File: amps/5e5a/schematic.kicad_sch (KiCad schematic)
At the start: 63 parts, among them T1 PT, T2 ~4.3k:8

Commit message: Fix: the 6G5's rectifier was connected to nothing; 17 sheets shorted the mains by naming both leads alike
6G5 power supply. The sheet drew four diodes as a "silicon bridge" whose
HT_A/HT_B labels stopped 6 mm short of their wires. D1/D2's anodes sat on
the tremolo's cathode node (a tremolo wire's end touched the old diode
stub), D3/D4 ran from ground to the reservoir, and TR1's centre tap floated
under an open-pin waiver whose stated reason was the bridge itself.
A-FJ (Schematic Heaven 2153x1437, read enlarged): each HT end of TR1 runs
through a leg of three silicon diodes, every + (cathode) toward the +460 V
reservoir; the centre tap is grounded; TR1's second secondary terminal is a
bias tap feeding the 6G4's network part for part: rectifier, 8-150, 10K,
then 8-150 and a 56K bleeder at the -55 V line. Redrawn as the drawing
shows: D1-D6, TR1 with its tap pin, the centre tap to ground, the bias
network (CBIAS 25 uF -> 8 uF; RBIAS2, CBIAS2, RBIAS1 added), the waiver
deleted, and the notes, meta, netlist header and parts list no longer say
bridge. Not yet carried: the drawing's second 20-600 at the reservoir and
the standby switch (this sheet omits chassis switches by its own note);
and the tremolo ladder still runs through the transformer's corner of the
sheet, a layout clash rather than a connection, queued for its own redraw.

Mains. Two global labels with one name are one net. 16 of 24 power
transformers on the sheets carried a label named MAINS on both primary
leads, so the winding's two pins were one net: 5E4-A, 5E5-A, 5F4, 5G9,
6161, 6G2, 6G3, 6G4, AA1164, AA764, AA764-Vibro, AA964, AB763, AB763
Super, AB763 Twin, GA-40. The 6G5's loop ran from one MAINS label through
switch, fuse and winding back to the same name. No gate models the primary,
so a copy-pasted idiom did this. The second lead is now MAINS N, the AC15's
idiom; the AA1164's and AA964's second AC row, drawn under the first row's
name, is the neutral. The death and across-the-line caps stay on the le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
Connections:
- net MAINS: no longer T1.2 (PRI_2)
- new net MAINS N: T1.2 (PRI_2)
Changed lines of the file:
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@@
   (wire (pts (xy 188.31 142.78) (xy 184.31 142.78))
     (stroke (width 0) (type default)))
-  (global_label "MAINS" (shape input) (at 184.31 142.78 180)
+  (global_label "MAINS N" (shape input) (at 184.31 142.78 180)
     (effects (font (size 1.27 1.27)) (justify right)))
   (wire (pts (xy 206.09 132.62) (xy 218.09 132.62))

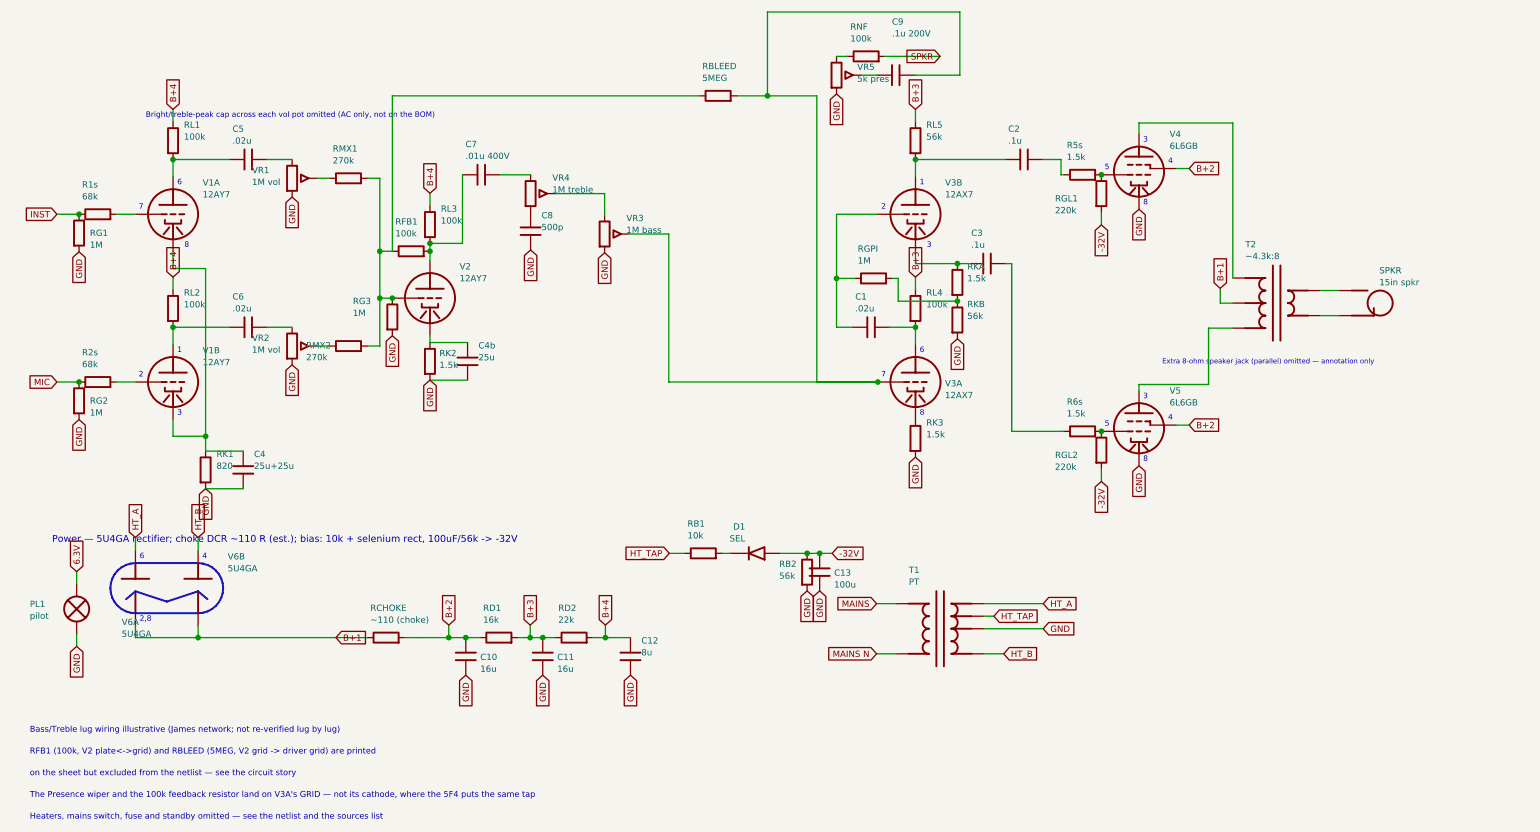
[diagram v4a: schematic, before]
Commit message: Fix: the 5E5-A sheet draws V2 as a gain stage into a cathode follower, and the tone network off the follower's cathode
V2A (unit 2, pins 1-2-3 on the layout page) is DC-coupled into V2B (unit 1,
pins 6-7-8), the follower. Its cathode drives the split treble/bass network
the 5F4 also draws, part for part as J-EE letters it. RF1, the 5 MEG, runs
from the mixing node over the top of the stage to the bass branch. The 100K
feedback and the Presence rheostat now land on the driver's cathode, and a
SPKR flag on the output secondary ties RNF to the speaker. V3's units follow
the layout page (driver on 1-2-3, cathodyne on 6-7-8). The bright cap and the
+390 V can are drawn, and the droppers are lettered 10k.

Gates: verify_schematic_nets PASS (claimed), check_schematics clean,
check_value_consistency agrees, check_tonestack_wiring 0 failures.

Co-Authored-By: Claude Opus 5 (1M context) <noreply@anthropic.com>
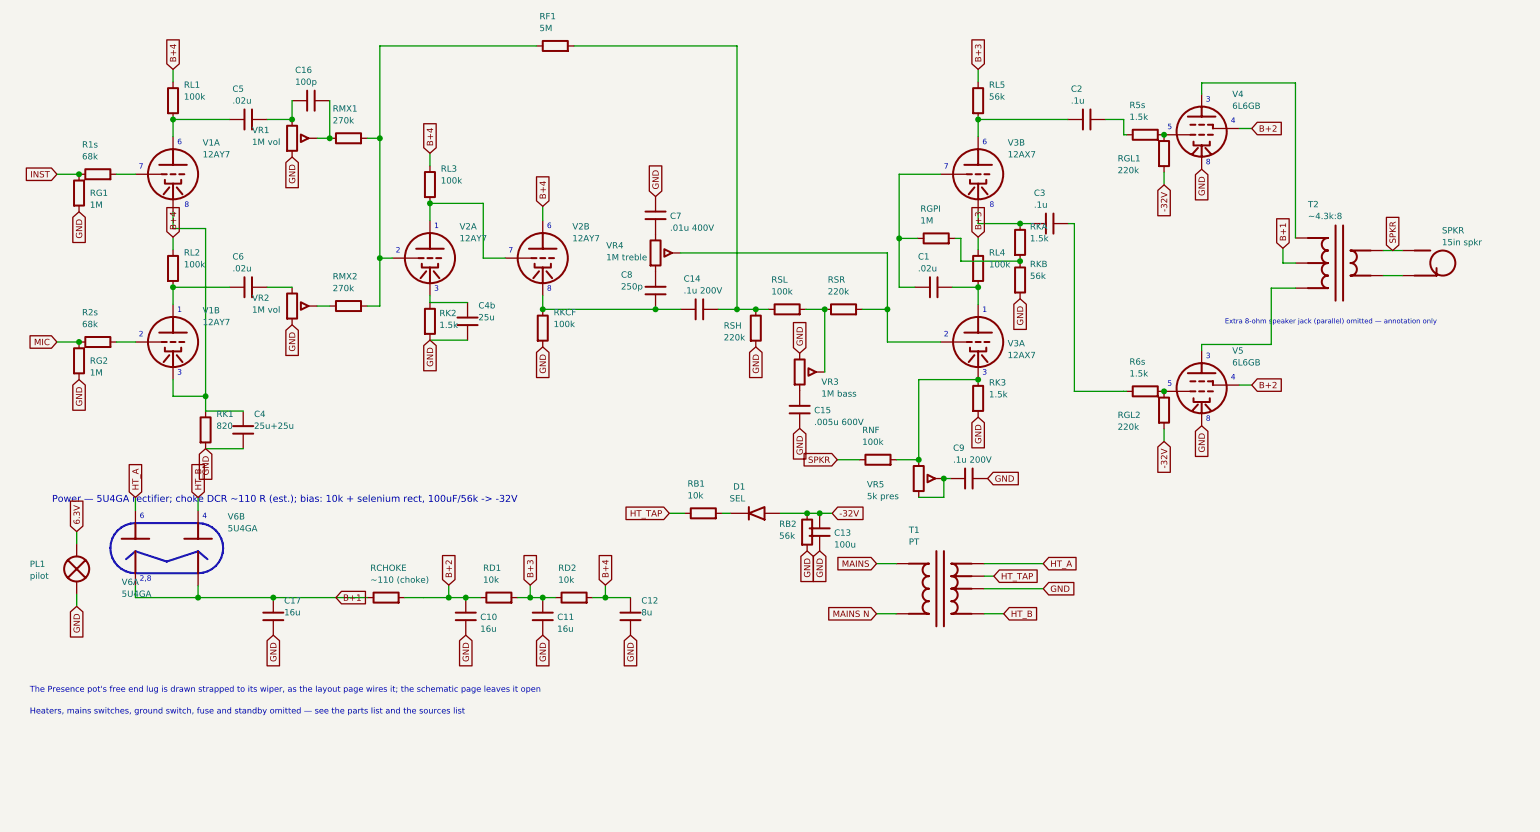
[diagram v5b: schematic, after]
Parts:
- removed C10: 16u, symbol cx:C
- removed C7: .01u 400V, symbol cx:C
- removed RBLEED: 5MEG, symbol cx:R
- removed RFB1: 100k, symbol cx:R
- removed RG3: 1M, symbol cx:R
- removed RL5: 56k, symbol cx:R
- removed V2: 12AY7, symbol cx:TRIODE
- added C1: .02u, symbol cx:C
- added C11: 16u, symbol cx:C
- added C14: .1u 200V, symbol cx:C
- added C15: .005u 600V, symbol cx:C
- added C16: 100p, symbol cx:C
- added D1: SEL, symbol cx:DIODE_SS
- added RF1: 5M, symbol cx:R
- added RK2: 1.5k, symbol cx:R
- added RKCF, RNF, RSL: 100k, symbol cx:R
- added RSH: 220k, symbol cx:R
- added V2B: 12AY7, symbol cx:TRIODE
- added VR3: 1M bass, symbol cx:POT
- C10: renamed from D1; value SEL -> 16u; symbol cx:DIODE_SS -> cx:C
- C7: renamed from VR3; value 1M bass -> .01u 400V; symbol cx:POT -> cx:C
- C8: value 500p -> 250p
- RD1: value 16k -> 10k
- RD2: value 22k -> 10k
- RK3: renamed from C1; value .02u -> 1.5k; symbol cx:C -> cx:R
- RL5: renamed from RK3; value 1.5k -> 56k
- RSR: renamed from RNF; value 100k -> 220k
- V2A: renamed from RK2; value 1.5k -> 12AY7; symbol cx:R -> cx:TRIODE; Basing_unit (none) -> 2
- V3A: Basing_unit (none) -> 2
- V3B: Basing_unit (none) -> 1
- renumbered C11 to C17
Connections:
- net -32V: now also D1.1 (A); no longer C10.1 (A)
- net B+1: now also C17.1
- net B+2: now also C10.1
- net B+3: now also RL5.1, C11.1; no longer C17.1
- net B+4: now also V2B.1 (P)
- net GND: now also C10.2, C7.1, C9.2, RK3.2, C11.2, C15.2, RK2.2, RKCF.2, RSH.2, VR3.1; no longer C7.3, C8.2, RL5.2, V2A.2, VR5.3
- net SPKR: now also SPKR.1 (T), T2.4 (SEC_H), RNF.1; no longer RSR.2
- net at C2.1, V3B.1 (P): now also RL5.2
- net at RGPI.1, V3B.2 (G): now also C1.1; no longer RK3.1
- net at RB1.2: now also D1.2 (K); no longer C10.2 (K)
- net at RMX1.2, RMX2.2: now also V2A.2 (G), RF1.1
- net at RL4.2, V3A.1 (P): now also C1.2; no longer RK3.2
- net at VR4.2 (W): now also RSR.2, V3A.2 (G); no longer C7.1
- net at VR4.1: now also C7.2
- net at RL3.2: now also V2A.1 (P), V2B.2 (G)
- net at C4b.1: now also V2A.3 (K), RK2.1; no longer V2A.1
- net at V3A.3 (K): now also RK3.1, VR5.1, RNF.2; no longer RL5.1
- net at C9.1, VR5.2 (W): now also VR5.3
- net at C5.2, VR1.1: now also C16.1
- net at RMX1.1, VR1.2 (W): now also C16.2
- net at RSR.1: now also RSL.2, VR3.2 (W); no longer VR5.1
- new net: C14.1, C8.2, RKCF.1, V2B.3 (K)
- new net: C14.2, RF1.2, RSH.1, RSL.1
- new net: C15.1, VR3.3
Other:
- note added: "Heaters, mains switches, ground switch, fuse and standby omitted — see the parts list and the sources list"
- note added: "The Presence pot's free end lug is drawn strapped to its wiper, as the layout page wires it; the schematic page leaves it open"
- note removed: "Bass/Treble lug wiring illustrative (James network; not re-verified lug by lug)"
- note removed: "Bright/treble-peak cap across each vol pot omitted (AC only, not on the BOM)"
- note removed: "Heaters, mains switch, fuse and standby omitted — see the netlist and the sources list"
- note removed: "RFB1 (100k, V2 plate<->grid) and RBLEED (5MEG, V2 grid -> driver grid) are printed"
- note removed: "The Presence wiper and the 100k feedback resistor land on V3A's GRID — not its cathode, where the 5F4 puts the same tap"
- note removed: "on the sheet but excluded from the netlist — see the circuit story"
- moved on the sheet: C10, C17, C5, R1s, RG1, RL1, RL5, RMX1, RSR, V1A, VR1

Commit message: 5E5-A: each input jack has its own 68 kΩ stopper
J-EE (the cited Schematic Heaven copy, sha1 18c0ebb5, both pages
1506x864) draws four input jacks and four 68 Ks, two per channel, with one
1 MEG per channel at jack 1's tip and jack 2's contact resting on jack 1's
tip: schematic crop 0,210,210,630; layout crop 1180,110,1420,480, where the
board carries four 68 K bodies. The BOM note called one stopper per channel
a "representative" simplification and cited the 5E3 note as precedent; that
note was itself wrong and was fixed in f422a73. R3s and R4s (68 k) are
added to the BOM, the sheet and the board (declared series_bridge); the
board widens by two columns and its caption drops the "collapse to two".
No DC node moves. The amp is a draft; status untouched.

Co-Authored-By: Claude Opus 5.5 <noreply@anthropic.com>
Claude-Session: https://claude.ai/code/session_01KBMfdh37HmCL2iWcBiL5J1
Signed-off-by: AnalogMaker <theanalogmaker@gmail.com>
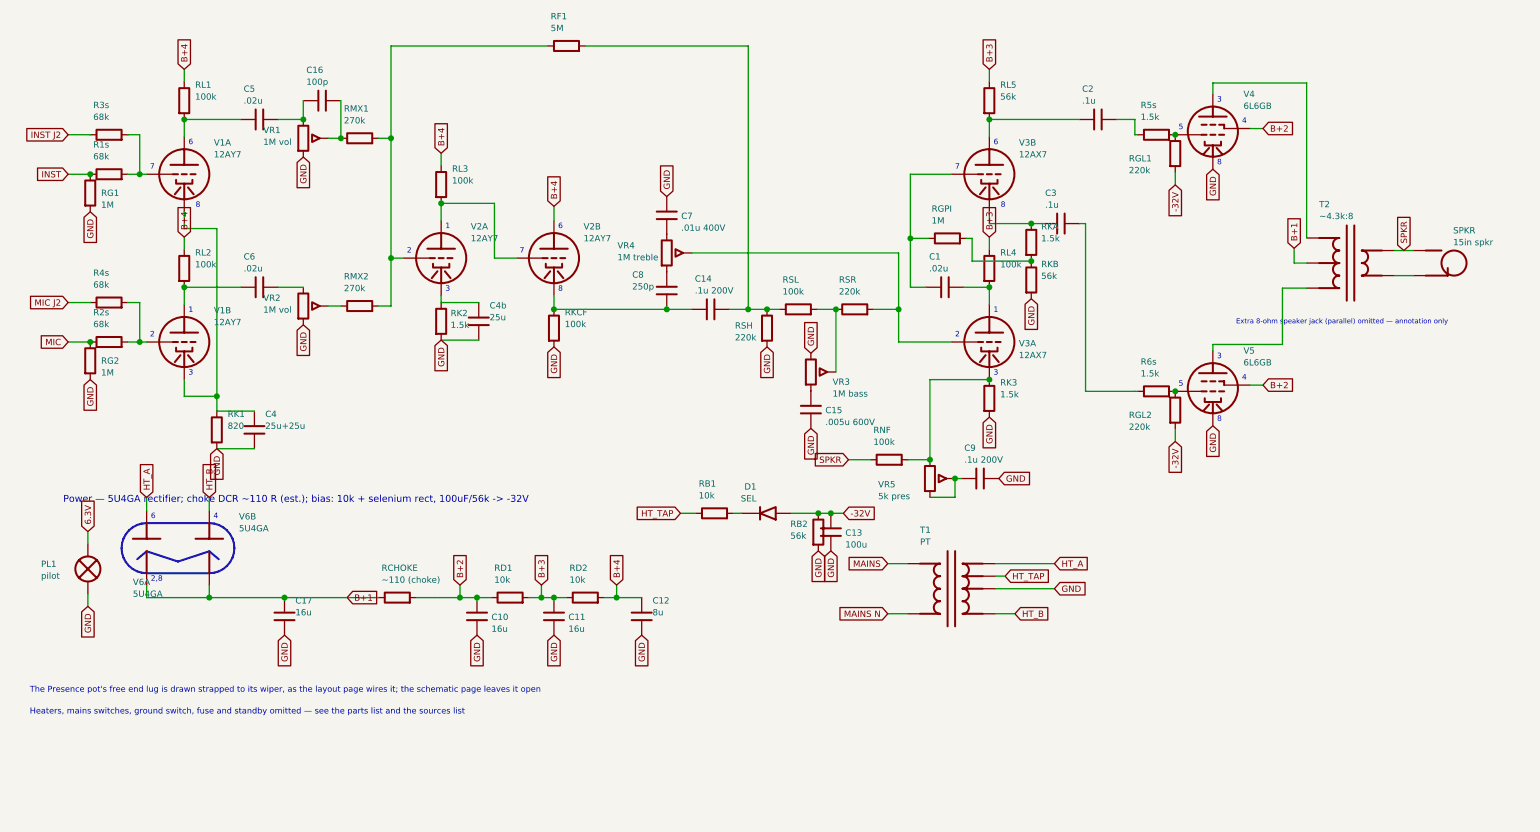
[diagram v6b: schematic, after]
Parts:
- removed C11, C17: 16u, symbol cx:C
- removed C12: 8u, symbol cx:C
- removed C14: .1u 200V, symbol cx:C
- removed C16: 100p, symbol cx:C
- removed C8: 250p, symbol cx:C
- removed RB1: 10k, symbol cx:R
- removed RK1: 820, symbol cx:R
- removed RKCF, RL1: 100k, symbol cx:R
- removed SPKR: 15in spkr, symbol cx:JACK
- removed V2A: 12AY7, symbol cx:TRIODE
- removed V3A: 12AX7, symbol cx:TRIODE
- added C10: 16u, symbol cx:C
- added C13: 100u, symbol cx:C
- added D1: SEL, symbol cx:DIODE_SS
- added R3s, R4s: 68k, symbol cx:R
- added RKA: 1.5k, symbol cx:R
- added RL3: 100k, symbol cx:R
- added RSH, RSR: 220k, symbol cx:R
- added T1: PT, symbol cx:PT
- added V1B, V2B: 12AY7, symbol cx:TRIODE
- added V6A: 5U4GA, symbol cx:DIODE_TUBE
- added VR1: 1M vol, symbol cx:POT
- added VR3: 1M bass, symbol cx:POT
- C1: renamed from RKA; value 1.5k -> .02u; symbol cx:R -> cx:C
- C11: renamed from D1; value SEL -> 16u; symbol cx:DIODE_SS -> cx:C
- C12: renamed from C13; value 100u -> 8u
- C14: renamed from VR3; value 1M bass -> .1u 200V; symbol cx:POT -> cx:C
- C16: renamed from V1B; value 12AY7 -> 100p; symbol cx:TRIODE -> cx:C
- C8: renamed from RSR; value 220k -> 250p; symbol cx:R -> cx:C
- RB1: renamed from T1; value PT -> 10k; symbol cx:PT -> cx:R
- RK1: renamed from RL3; value 100k -> 820
- RKCF: renamed from RSH; value 220k -> 100k
- RL1: renamed from VR1; value 1M vol -> 100k; symbol cx:POT -> cx:R
- SPKR: renamed from V6A; value 5U4GA -> 15in spkr; symbol cx:DIODE_TUBE -> cx:JACK
- V2A: renamed from V2B; Basing_unit 1 -> 2
- V3A: renamed from C1; value .02u -> 12AX7; symbol cx:C -> cx:TRIODE; Basing_unit (none) -> 2
- renumbered C10 to C17
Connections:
- net -32V: now also C13.1, D1.1 (A); no longer C11.1 (A), C12.1
- net B+1: now also C17.1, V6A.2 (K); no longer SPKR.2 (K)
- net B+2: now also C10.1; no longer C17.1
- net B+3: now also C11.1
- net B+4: now also C12.1, RL1.1, RL3.1, V2B.1 (P); no longer RK1.1, V2A.1 (P)
- net GND: now also C11.2, RK1.2, C10.2, C13.2, RSH.2, T1.4 (HT_CT), VR1.3, VR3.1; no longer C14.1, RB1.4 (HT_CT), RL1.3
- net HT_A: now also T1.3 (HT_A), V6A.1 (A); no longer RB1.3 (HT_A), SPKR.1 (A)
- net HT_B: now also T1.5 (HT_B); no longer RB1.5 (HT_B)
- net HT_TAP: now also RB1.1, T1.6 (HT_TAP); no longer RB1.6 (HT_TAP)
- net MAINS: now also T1.1 (PRI_1); no longer RB1.1 (PRI_1)
- net MAINS N: now also T1.2 (PRI_2); no longer RB1.2 (PRI_2)
- net SPKR: now also SPKR.1 (T)
- net at C4b.1, RK2.1: now also V2A.3 (K)
- net at RGPI.1, V3B.2 (G): now also C1.1; no longer V3A.1
- net at RGPI.2, RKB.1: now also RKA.2; no longer C1.2
- net at C16.2: now also RMX1.1, VR1.2 (W); no longer R2s.2
- net at RF1.2, RSL.1: now also C14.2, RSH.1; no longer RKCF.1
- net at T2.5 (SEC_C): now also SPKR.2 (S)
- net at C3.1, V3B.3 (K): now also RKA.1; no longer C1.1
- net at C5.2: now also C16.1, VR1.1; no longer RL1.1
- net at RL1.2: now also C5.1, V1A.1 (P); no longer RMX1.1
- net at V2A.2 (G): now also RF1.1, RMX1.2, RMX2.2; no longer RK1.2
- net at C4.1, V1A.3 (K): now also RK1.1, V1B.3 (K); no longer C16.3 (K)
- net at RK3.1, RNF.2, VR5.1: now also V3A.3 (K)
- net at C6.1, RL2.2: now also V1B.1 (P); no longer C16.1 (P)
- net at RL4.2: now also C1.2, V3A.1 (P); no longer V3A.2
- net at C8.2: now also C14.1, RKCF.1, V2B.3 (K); no longer VR4.2 (W)
- net at VR4.3: now also C8.1
- net at R1s.2, V1A.2 (G): now also R3s.2
- net at C15.1: now also VR3.3; no longer C14.3
- new net: RSL.2, RSR.1, VR3.2 (W)
- new net: RL3.2, V2A.1 (P), V2B.2 (G)
- new net: D1.2 (K), RB1.2
- new net: RSR.2, V3A.2 (G), VR4.2 (W)
- new net: R2s.2, R4s.2, V1B.2 (G)
- new net INST J2: R3s.1
- new net MIC J2: R4s.1
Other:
- moved on the sheet: C11, C12, C17, R1s, RK1, RKCF, V1A, V2A
